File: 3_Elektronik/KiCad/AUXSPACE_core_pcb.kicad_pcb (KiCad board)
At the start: 4 copper layers, 60 x 60 mm, 83 parts, among them J1 Conn_02x10_Odd_Even, J2 Conn_02x10_Odd_Even, J3 Conn_02x10_Odd_Even, J4 Conn_02x10_Odd_Even, J5 PinHeader 2,54mm 3p, J6 693072010801, J7 629722000214, Q1 2N7002K, Q2 2N7002K, SW2 430481025816, SW3 430481025816, U1 ADXL375BCCZ, U2 TPS7B8601QDDARQ1, U3 TCAN334, U4 ESP32-S3-WROOM-1, U5 LSM6DSO32XTR, U6 DPS310, U7 MLX90395xLW, U8 CH224A

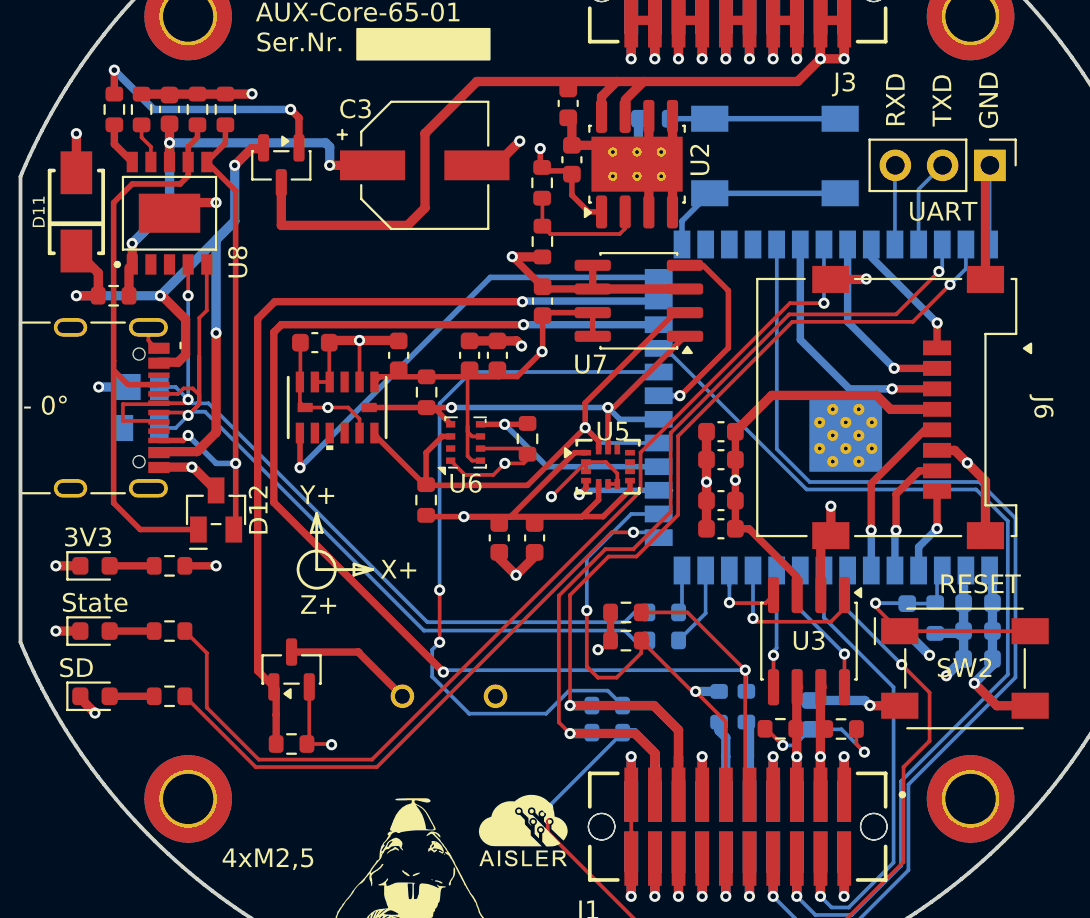
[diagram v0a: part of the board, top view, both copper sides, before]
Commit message: fix: :bug: drc errors
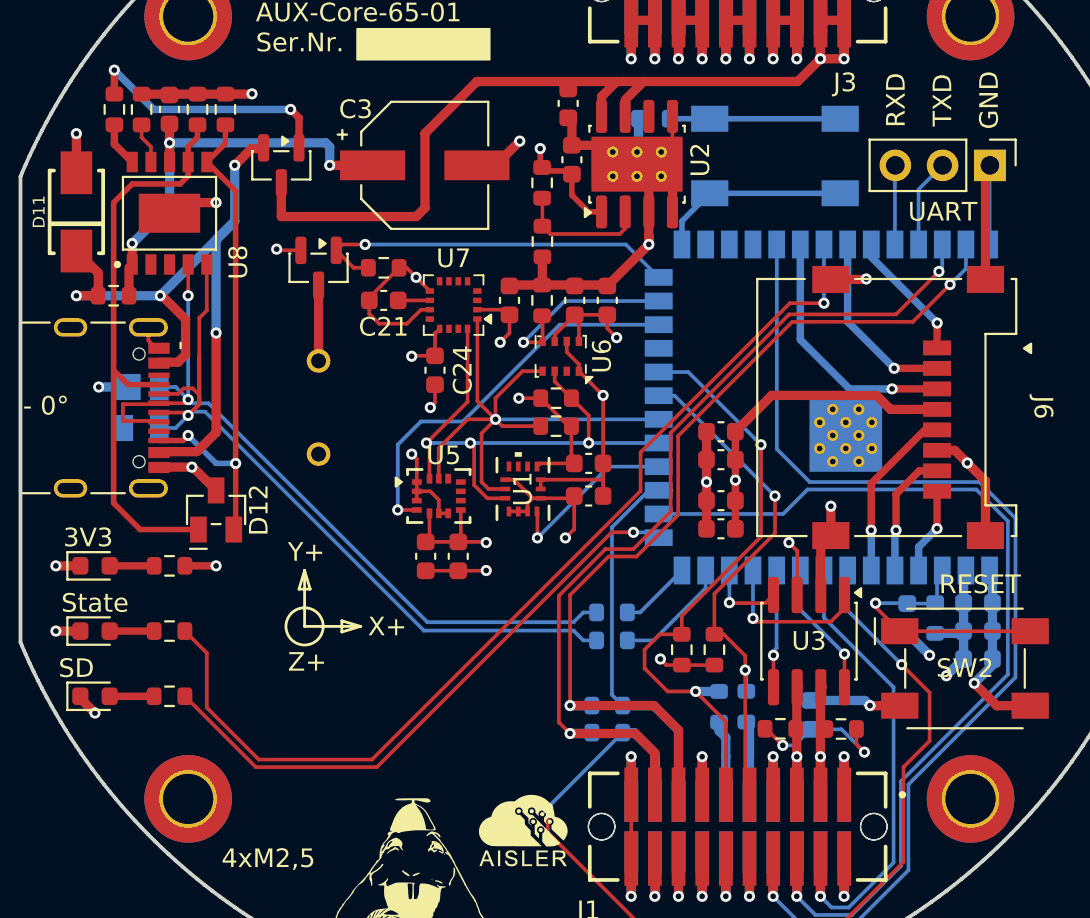
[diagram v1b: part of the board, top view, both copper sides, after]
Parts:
- removed the G*** at (142.8, 77.5)
- removed the G*** at (142.0, 122.5)
- added ?: LOGO, AUXSPACE:stack_pwr, B.Cu at (141.0, 79.0)
- added ?: LOGO, AUXSPACE:stack_data, B.Cu at (141.0, 121.0)
- added C21: 4.7µF, Capacitor_SMD:C_0603_1608Metric, F.Cu at (139.5, 94.2)
- added C24: 100nF, Capacitor_SMD:C_0603_1608Metric, F.Cu at (142.2, 98.0)
- C23: value 1µF -> 100nF
- U1: value ADXL375BCCZ -> LSM6DSV320XTR; footprint AUXSPACE:LGA_CC-14-1_ADI -> AUXSPACE:LGA-14L_2p5X3X0p83_STM
- U7: value MLX90395xLW -> IST8310; footprint Package_SO:SOIC-8_3.9x4.9mm_P1.27mm -> Package_LGA:LGA-16_3x3mm_P0.5mm
- moved R11 26.0 mm to (139.5, 92.5)
- moved Q1 21.6 mm to (136.0, 92.5), turned to -90 degrees
- moved BZ1 17.0 mm to (136.0, 100.0), turned to 90 degrees
- moved C23 16.8 mm to (150.5, 104.8)
- moved C22 11.7 mm to (150.5, 103.0), turned to 180 degrees
- moved U1 10.9 mm to (147.0, 104.4), turned to 90 degrees
- moved U7 9.95 mm to (143.2, 94.5)
- moved U5 9.22 mm to (142.5, 104.8)
- moved R10 8.86 mm to (148.8, 99.5), turned to 180 degrees
- moved R12 7.47 mm to (148.0, 94.2), turned to -90 degrees
- moved R9 7.18 mm to (148.8, 101.0), turned to 0 degrees
- moved U6 6.89 mm to (149.0, 97.2), turned to 180 degrees
- moved C6 6.60 mm to (151.5, 94.2)
- moved C5 6.37 mm to (149.8, 94.2)
- moved R16 5.15 mm to (157.2, 113.0), turned to -90 degrees
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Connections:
- C20 pad 1: GND -> +3V3
- C20 pad 2: +3V3 -> GND
- U1 pad 13: /Baseboard/I2C0_SDA -> /Baseboard/I2C0_SCL
- U1 pad 14: /Baseboard/I2C0_SCL -> /Baseboard/I2C0_SDA
- U1 pad 2: GND -> +3V3
- U1 pad 3: unconnected-(U1-RESERVED-Pad3) -> +3V3
- U1 pad 4: GND -> /Baseboard/ACCEL_INT1
- U1 pad 5: GND -> +3V3
- U1 pad 6: +3V3 -> GND
- U1 pad 7: +3V3 -> GND
- U1 pad 8: /Baseboard/ACCEL_INT -> +3V3
- U1 pad 9: unconnected-(U1-INT2-Pad9) -> /Baseboard/ACCEL_INT2
- U4 pad 16: /Baseboard/I2C_SCL_top -> /Baseboard/LIFTOFF
- U4 pad 17: /Baseboard/IMU_INT -> /Baseboard/UART_TX_bot
- U4 pad 18: /Baseboard/BARO_INT -> /Baseboard/ACCEL_INT1
- U4 pad 21: /Baseboard/MAG_INT -> /Baseboard/I2C_SDA_top
- U4 pad 22: /Baseboard/UART_TX_bot -> /Baseboard/I2C_SCL_top
- U4 pad 23: /Baseboard/LIFTOFF -> unconnected-(U4-IO21-Pad23)
- U4 pad 24: /Baseboard/I2C_SDA_top -> /Baseboard/IMU_INT
- U4 pad 25: /Baseboard/Buzzer -> /Baseboard/BARO_INT
- U4 pad 26: /Baseboard/ACCEL_INT -> /Baseboard/Buzzer
- U5 pad 1: +3V3 -> GND
- U7 pad 2: /Baseboard/I2C0_SDA -> +3V3
- U7 pad 3: GND -> unconnected-(U7-NC-Pad3)
- U7 pad 4: /Baseboard/MAG_INT -> unconnected-(U7-NC-Pad4)
- U7 pad 5: GND -> unconnected-(U7-CAD0-Pad5)
- U7 pad 6: GND -> unconnected-(U7-CAD1-Pad6)
- U7 pad 7: +3V3 -> unconnected-(U7-VPP-Pad7)
- U7 pad 8: +3V3 -> unconnected-(U7-NC-Pad8)
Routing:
- net /Baseboard/I2C_SDA_top: track 74.0 -> 28.4 mm, vias 3 -> 2
- net /Baseboard/UART_TX_bot: track 47.4 -> 21.2 mm, vias 2 -> 0
- net /Baseboard/ACCEL_INT: track 25.4 -> 0.00 mm, vias 1 -> 0
- net /Baseboard/Buzzer: track 45.2 -> 20.3 mm
- net +3V3: track 95.6 -> 74.2 mm, vias 8 -> 12
- net /Baseboard/IMU_INT: track 5.94 -> 21.2 mm
- net /Baseboard/MAG_INT: track 10.8 -> 0.00 mm, vias 1 -> 0
- net /Baseboard/ACCEL_INT1: track 0.00 -> 9.53 mm, vias 0 -> 1
- net GND: track 223.5 -> 215.8 mm
- net /Baseboard/I2C_SCL_top: track 26.7 -> 33.1 mm
- net /Baseboard/I2C0_SCL: track 25.5 -> 31.9 mm, vias 2 -> 1
- net Net-(BZ1--): track 7.02 -> 4.06 mm
- net /Baseboard/USB_D-: track 48.2 -> 45.5 mm
- net /Baseboard/USB_D+: track 45.4 -> 42.7 mm
- net /Baseboard/LIFTOFF: track 55.0 -> 52.4 mm
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
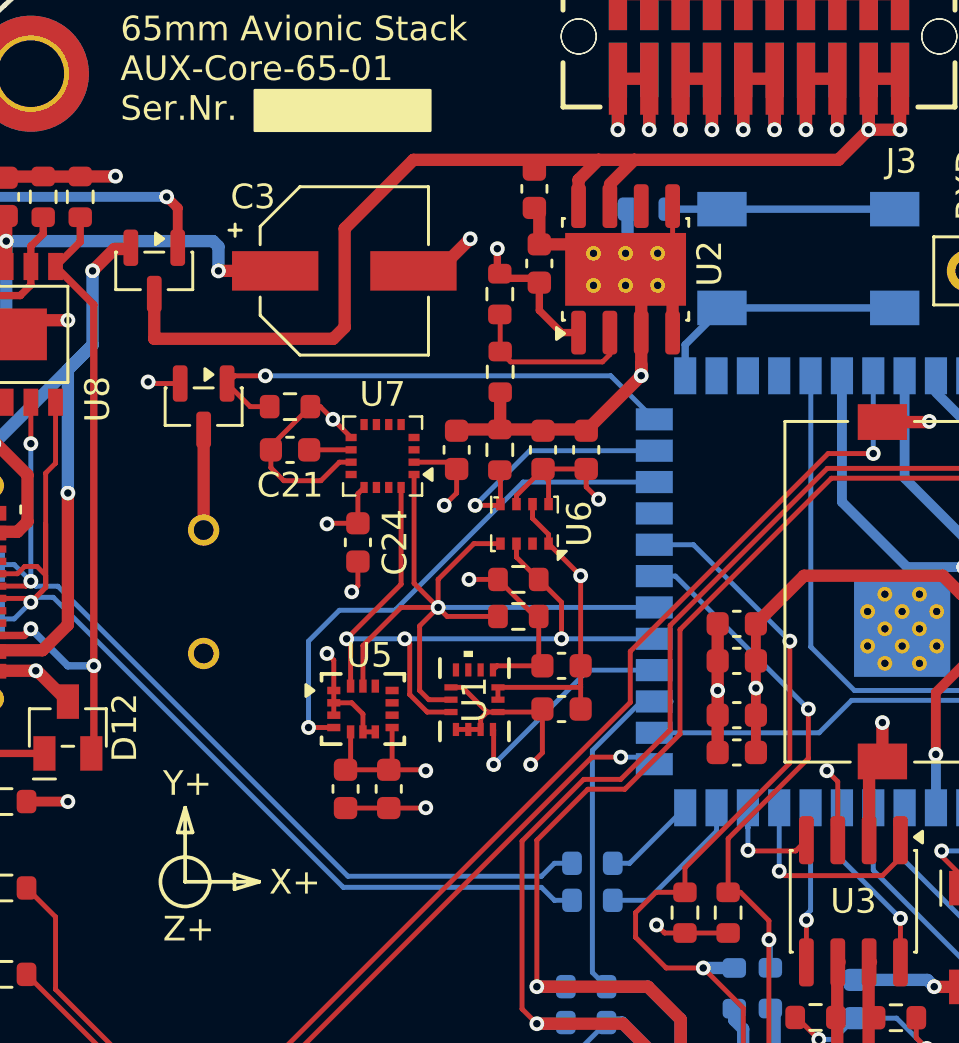
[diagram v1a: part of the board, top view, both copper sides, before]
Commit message: fix: :bug: use LIS3MDL mag
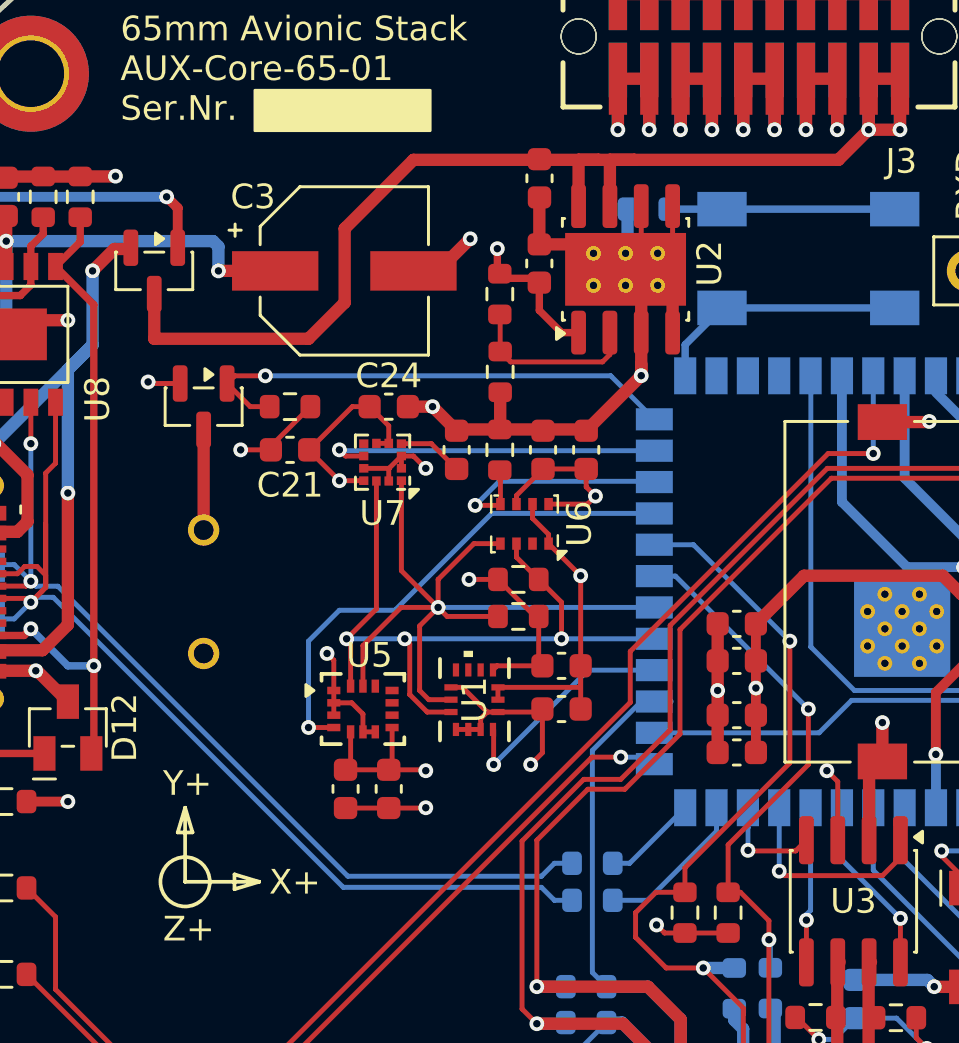
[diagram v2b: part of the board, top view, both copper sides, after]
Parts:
- C21: value 4.7µF -> 1µF
- U7: value IST8310 -> LIS3MDL; footprint Package_LGA:LGA-16_3x3mm_P0.5mm -> Package_LGA:LGA-12_2x2mm_P0.5mm
- moved C24 5.64 mm to (143.5, 92.5), turned to 0 degrees
- moved C4 0.47 mm to (149.6, 83.2)
- moved U7 0.25 mm to (143.2, 94.8)
- turned C20 to -90 degrees
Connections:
- C20 pad 1: +3V3 -> GND
- C20 pad 2: GND -> Net-(U7-C1)
- C21 pad 1: Net-(U7-C1) -> +3V3
- C24 pad 1: GND -> +3V3
- C24 pad 2: +3V3 -> GND
- U4 pad 23: unconnected-(U4-IO21-Pad23) -> /Baseboard/IMU_INT
- U4 pad 24: /Baseboard/IMU_INT -> /Baseboard/BARO_INT
- U4 pad 25: /Baseboard/BARO_INT -> /Baseboard/MAG_DRDY
- U7 pad 10: Net-(U7-C1) -> +3V3
- U7 pad 11: GND -> /Baseboard/I2C0_SDA
- U7 pad 12: unconnected-(U7-NC-Pad12) -> GND
- U7 pad 2: +3V3 -> GND
- U7 pad 3: unconnected-(U7-NC-Pad3) -> GND
- U7 pad 4: unconnected-(U7-NC-Pad4) -> Net-(U7-C1)
- U7 pad 5: unconnected-(U7-CAD0-Pad5) -> +3V3
- U7 pad 6: unconnected-(U7-CAD1-Pad6) -> +3V3
- U7 pad 8: unconnected-(U7-NC-Pad8) -> /Baseboard/MAG_DRDY
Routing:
- net /Baseboard/MAG_DRDY: track 0.00 -> 13.9 mm, vias 0 -> 1
- net +3V3: track 74.2 -> 76.5 mm, vias 12 -> 11
- net GND: track 215.8 -> 217.9 mm, vias 39 -> 40
- net Net-(U7-C1): track 1.70 -> 2.66 mm
- net /Baseboard/BARO_INT: track 11.0 -> 10.5 mm

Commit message: ci(drc): :green_heart: fix errors
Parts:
- U4: footprint RF_Module:ESP32-S3-WROOM-1 -> AUXSPACE:ESP32-S3-WROOM-1
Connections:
- net /Baseboard/CAN+ renamed /Baseboard/CAN_H
- net /Baseboard/CAN- renamed /Baseboard/CAN_L
- net /Baseboard/VBus_Switched_D renamed /Baseboard/VBus_switched_D
- U1 pad 9: /Baseboard/ACCEL_INT2 -> unconnected-(U1-INT2-Pad9)

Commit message: feat: :sparkles: new switches
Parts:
- J5: value PinHeader 2,54mm 3p -> Conn_01x04_Pin; footprint Connector_PinHeader_2.54mm:PinHeader_1x03_P2.54mm_Vertical -> Connector_PinHeader_2.54mm:PinHeader_1x04_P2.54mm_Vertical
- R23: moved to F.Cu
- SW2: value 430481025816 -> 434331013822; footprint AUXSPACE:SW_Wurth_WS-TASV_430481025816 -> AUXSPACE:SW_Wurth_WS-TASU_434331013822
- SW3: value 430481025816 -> 434331013822; footprint AUXSPACE:SW_Wurth_WS-TASV_430481025816 -> AUXSPACE:SW_Wurth_WS-TASU_434331013822; moved to F.Cu
- moved SW2 49.0 mm to (122.0, 108.8), turned to -90 degrees
- moved SW3 38.8 mm to (122.0, 91.2), turned to -90 degrees
- moved R23 30.5 mm to (123.5, 84.0), turned to -90 degrees
- moved D11 15.0 mm to (133.8, 100.0), turned to 0 degrees
- moved Q1 13.5 mm to (135.2, 106.0)
- moved BZ1 13.3 mm to (137.0, 113.2), turned to 0 degrees
- moved R11 11.3 mm to (135.2, 103.0), turned to 180 degrees
- moved C4 9.66 mm to (159.2, 83.8), turned to 0 degrees
- moved D3 7.04 mm to (126.7, 115.0)
- moved R18 6.79 mm to (130.0, 115.0)
- moved C11 5.52 mm to (146.2, 91.1), turned to 90 degrees
- moved R4 3.13 mm to (148.0, 91.1)
- moved D5 3.07 mm to (126.7, 117.0)
- moved D4 2.89 mm to (126.7, 113.0)
- moved R22 2.47 mm to (130.0, 117.0)
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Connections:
- J5 pad 2: /Baseboard/TX -> VBus_direct
- J5 pad 3: /Baseboard/RX -> /Baseboard/TX
- SW2 pad 1: Net-(U4-EN) -> GND
- SW2 pad 2: Net-(U4-EN) -> GND
- SW2 pad 3: GND -> Net-(U4-EN)
- SW2 pad 4: GND -> Net-(U4-EN)
- U4 pad 31: /Baseboard/Power Fault -> /Baseboard/STATE_LED
- U4 pad 32: /Baseboard/SD_CMD_MOSI -> /Baseboard/Power Fault
- U4 pad 33: /Baseboard/STATE_LED -> /Baseboard/SD_CMD_MOSI
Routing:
- net Net-(U4-EN): track 13.4 -> 58.3 mm, vias 1 -> 4
- net /Baseboard/IO0: track 10.4 -> 38.8 mm, vias 0 -> 1
- net GND: track 217.7 -> 245.9 mm, vias 40 -> 35
- net +3V3: track 76.5 -> 87.0 mm, vias 11 -> 12
- net Vusb: track 40.8 -> 30.9 mm, vias 4 -> 3
- net /Baseboard/STATE_LED: track 53.4 -> 45.1 mm
- net /Baseboard/Buzzer: track 20.3 -> 27.8 mm
- net VBus_direct: track 53.1 -> 58.9 mm
- net /Baseboard/SD_LED: track 32.3 -> 28.2 mm
- net Net-(BZ1--): track 4.06 -> 8.07 mm
- net /Baseboard/USB_D-: track 45.5 -> 42.9 mm
- net /Baseboard/SD_CMD_MOSI: track 13.5 -> 11.7 mm
- net /Baseboard/LIFTOFF: track 52.4 -> 54.2 mm
- net /Baseboard/CC2: track 27.6 -> 29.2 mm
- net /Baseboard/Power Fault: track 60.0 -> 61.6 mm
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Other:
- board text added: "5V"

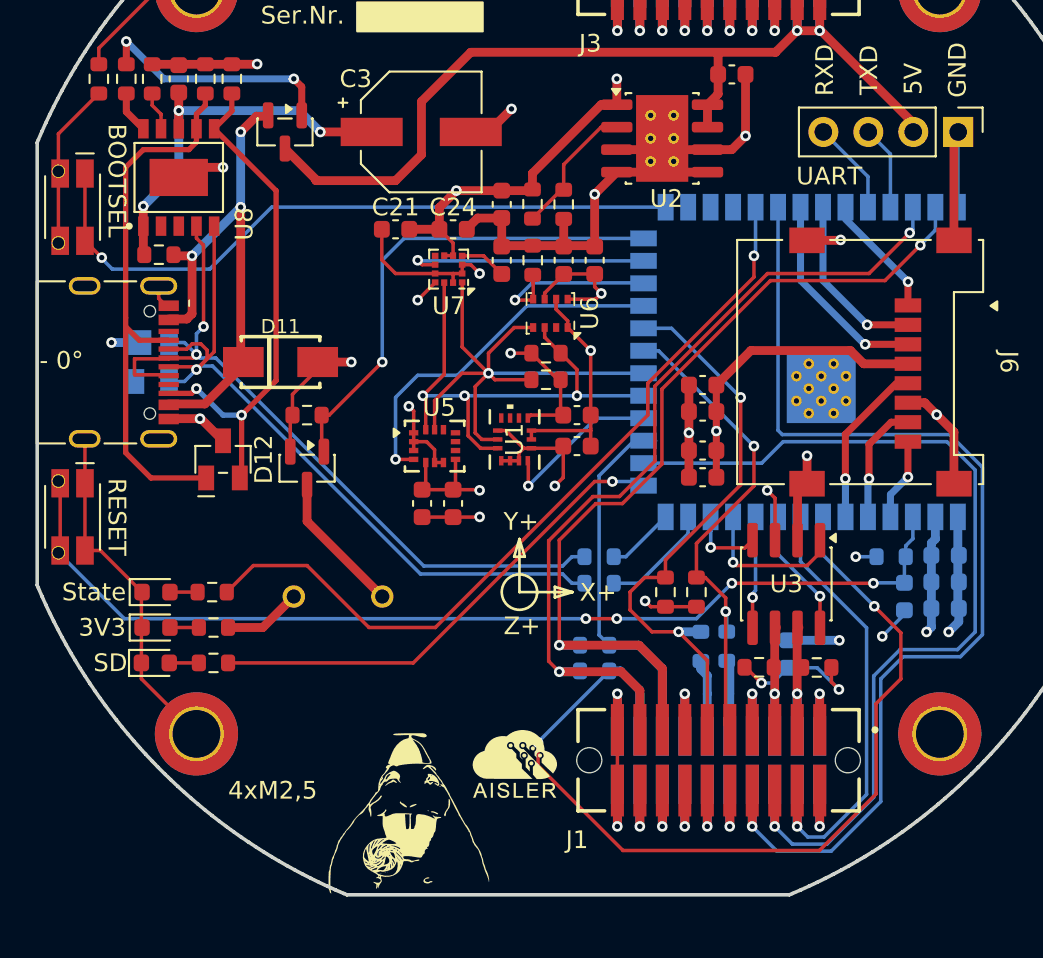
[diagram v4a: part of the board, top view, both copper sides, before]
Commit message: feat: :sparkles: add auxolotl
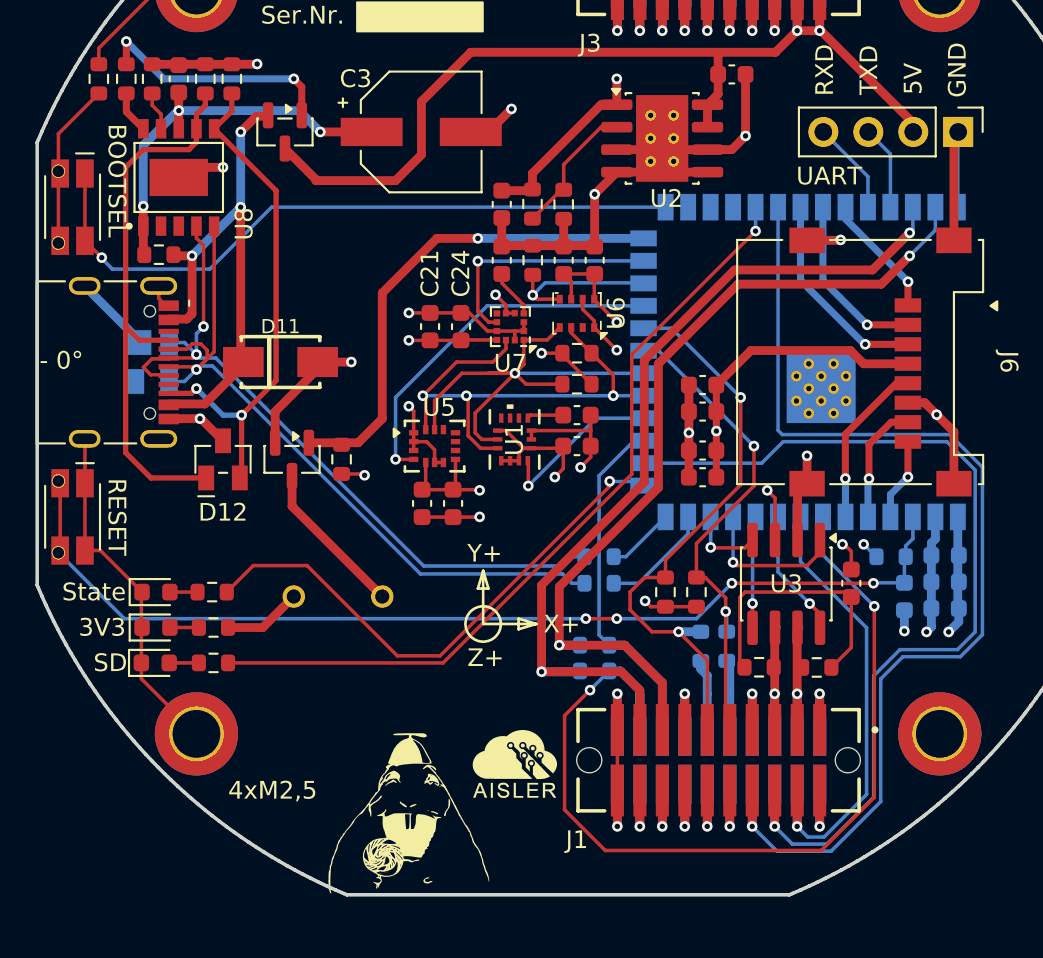
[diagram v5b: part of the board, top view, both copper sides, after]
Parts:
- added G***: LOGO, AUXSPACE:auxolotl, B.Cu at (141.0, 100.0)
- C16: moved to F.Cu
- moved C21 5.84 mm to (142.2, 98.0), turned to 90 degrees
- moved C24 5.52 mm to (143.9, 98.0), turned to 90 degrees
- moved C16 5.38 mm to (166.0, 112.5)
- moved U7 4.77 mm to (146.7, 98.0)
- moved R11 3.17 mm to (137.2, 105.5), turned to -90 degrees
- moved R9 1.77 mm to (150.5, 101.2)
- moved R10 1.75 mm to (150.5, 99.5)
- moved U6 1.50 mm to (150.5, 97.2)
- moved Q1 0.99 mm to (134.4, 105.5)
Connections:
- U4 pad 15: /Baseboard/SD_LED -> /Baseboard/STATE_LED
- U4 pad 31: /Baseboard/STATE_LED -> /Baseboard/SD_LED
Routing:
- net /Baseboard/SD_LED: track 28.2 -> 45.2 mm
- net /Baseboard/STATE_LED: track 45.1 -> 30.9 mm
- net Net-(C16-Pad2): track 7.99 -> 15.1 mm, vias 2 -> 0
- net +3V3: track 87.0 -> 80.3 mm
- net GND: track 245.9 -> 242.6 mm, vias 35 -> 36
- net /Baseboard/UART_RX_top: track 47.7 -> 49.9 mm
- net /Baseboard/UART_RX_bot: track 53.0 -> 51.2 mm
- net /Baseboard/I2C0_SCL: track 31.8 -> 30.2 mm
- net /Baseboard/USB_D+: track 43.0 -> 41.5 mm
- net /Baseboard/BARO_INT: track 10.5 -> 9.37 mm
- net Net-(BZ1--): track 8.07 -> 8.92 mm
